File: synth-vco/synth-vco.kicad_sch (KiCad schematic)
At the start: 61 parts, among them J1 Conn_Coaxial, J2 Screw_Terminal_01x10, J3 Screw_Terminal_01x05, J4 Conn_Coaxial, U1 ADF4158, U2 BT09E, U3 ADP-2-10+, U4 DAT-15R5A-SP+, U5 OPA192IDGKT, Y3 CVCO55CW-0500-1000

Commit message: reorder: added components' footprints and symbols files to the repo directory instead of them being unorganized in my downloads folder
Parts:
- Y3: footprint CVCO55CW-0500-1000:XTAL_CVCO55CW-0500-1000 -> GPR_Radar_Footprints:XTAL_CVCO55CW-0500-1000
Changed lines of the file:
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@@
 			)
 		)
-		(property "Footprint" "CVCO55CW-0500-1000:XTAL_CVCO55CW-0500-1000"
+		(property "Footprint" "GPR_Radar_Footprints:XTAL_CVCO55CW-0500-1000"
 			(at 403.86 254 0)
 			(hide yes)
@@
 			)
 		)
-		(property "Datasheet" ""
+		(property "Datasheet" "https://www.crystek.com/Specification/CVCO55CW-0500-1000"
 			(at 403.86 254 0)
 			(hide yes)

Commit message: schematic-feat: made the schematic for external 12V buck to 6V + LDOs to 5V and 3V3 lines
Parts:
- added C23, C31: 4.7u, Capacitor_SMD:C_0603_1608Metric_Pad1.08x0.95mm_HandSolder, symbol Device:C
- added C24, C25, C27, C29, C30, C32: 10u, Capacitor_SMD:C_0603_1608Metric_Pad1.08x0.95mm_HandSolder, symbol Device:C
- added C26, C28: 22u, Capacitor_SMD:C_0603_1608Metric_Pad1.08x0.95mm_HandSolder, symbol Device:C
- added J5: Barrel_Jack, Connector_BarrelJack:BarrelJack_SwitchcraftConxall_RAPC10U_Horizontal, symbol Connector:Barrel_Jack
- added NT1: NetTie_2, NetTie:NetTie-2_SMD_Pad0.5mm, symbol Device:NetTie_2
- added R22: 10K, Resistor_SMD:R_0201_0603Metric_Pad0.64x0.40mm_HandSolder, symbol Device:R
- added R23: 2K, Resistor_SMD:R_0201_0603Metric_Pad0.64x0.40mm_HandSolder, symbol Device:R
- added R24, R25: 49.9K, Resistor_SMD:R_0201_0603Metric_Pad0.64x0.40mm_HandSolder, symbol Device:R
- added U6: TPSM53602RDAR, GPR_Radar_Footprints:IC_TPSM53603RDAR, symbol TPSM53602RDAR:TPSM53602RDAR
- added U7, U8: LT3045IMSE_TRPBF, GPR_Radar_Footprints:SOP65P490X110-13N, symbol LT3045IMSE_TRPBF:LT3045IMSE_TRPBF
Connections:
- net GND: now also C23.1, C24.1, C25.1, C26.1, C27.1, C28.1, C29.1, C30.1, C31.1, C32.1, J5.2, NT1.2, R24.2, R25.2, U6.10 (NC), U6.11 (NC), U6.15 (PGND), U6.15_1 (PGND), U6.15_10 (PGND), U6.15_11 (PGND), U6.15_2 (PGND), U6.15_3 (PGND), U6.15_4 (PGND), U6.15_5 (PGND), U6.15_6 (PGND), U6.15_7 (PGND), U6.15_8 (PGND), U6.15_9 (PGND), U6.3 (NC), U7.13 (EXP), U7.6 (ILIM), U7.9 (GND), U8.13 (EXP), U8.6 (ILIM), U8.9 (GND)
- net 12 renamed 12V
- net 5V renamed +5V_BT09E
- net +5V_BT09E: now also C32.2, U8.10 (OUTS), U8.11 (OUT), U8.12 (OUT); no longer U1.22 (VP)
- new net: NT1.1, R23.1, U6.12 (AGND)
- new net: R22.1, R23.2, U6.9 (FB)
- new net: C31.2, R25.1, U8.8 (SET)
- new net: C23.2, R24.1, U7.8 (SET)
- new net +12V_IN: C25.2, C27.2, J5.1, U6.1 (VIN), U6.14 (VIN), U6.2 (EN)
- new net +5V_VP: C24.2, U1.22 (VP), U7.10 (OUTS), U7.11 (OUT), U7.12 (OUT)
- new net +6V_PRE: C26.2, C28.2, C29.2, C30.2, R22.2, U6.7 (VOUT), U6.8 (VOUT), U7.1 (IN), U7.2 (IN), U7.3 (IN), U7.4 (EN/UV), U7.7 (PGFB), U8.1 (IN), U8.2 (IN), U8.3 (IN), U8.4 (EN/UV), U8.7 (PGFB)
- no-connect marks 0 -> 4

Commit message: add: boost 6V to 20V LT8570 schematic
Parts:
- added C33, C35, C38, C41, C44: 10u, Capacitor_SMD:C_0603_1608Metric_Pad1.08x0.95mm_HandSolder, symbol Device:C
- added C34, C36, C39, C42: 4.7u, Capacitor_SMD:C_0603_1608Metric_Pad1.08x0.95mm_HandSolder, symbol Device:C
- added C37, C40, C43: 0.47u, Capacitor_SMD:C_0603_1608Metric_Pad1.08x0.95mm_HandSolder, symbol Device:C
- added R26: 49.9K, Resistor_SMD:R_0201_0603Metric_Pad0.64x0.40mm_HandSolder, symbol Device:R
- added R27, R28, R29: 32.4K, Resistor_SMD:R_0201_0603Metric_Pad0.64x0.40mm_HandSolder, symbol Device:R
- added U10, U11, U12, U9: LT3045IMSE_TRPBF, GPR_Radar_Footprints:SOP65P490X110-13N, symbol LT3045IMSE_TRPBF:LT3045IMSE_TRPBF
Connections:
- net +6V_PRE: now also C33.2, C36.2, C39.2, C42.2, U10.1 (IN), U10.2 (IN), U10.3 (IN), U10.4 (EN/UV), U10.7 (PGFB), U11.1 (IN), U11.2 (IN), U11.3 (IN), U11.4 (EN/UV), U11.7 (PGFB), U12.1 (IN), U12.2 (IN), U12.3 (IN), U12.4 (EN/UV), U12.7 (PGFB), U9.1 (IN), U9.2 (IN), U9.3 (IN), U9.4 (EN/UV), U9.7 (PGFB)
- net 3V3: no longer FL1.2, U1.18 (SDVDD), U1.19 (DVDD), U1.6 (AVDD), U1.7 (AVDD), U1.8 (AVDD)
- net GND: now also C33.1, C34.1, C35.1, C36.1, C37.1, C38.1, C39.1, C40.1, C41.1, C42.1, C43.1, C44.1, R26.2, R27.2, R28.2, R29.2, U10.13 (EXP), U10.6 (ILIM), U10.9 (GND), U11.13 (EXP), U11.6 (ILIM), U11.9 (GND), U12.13 (EXP), U12.6 (ILIM), U12.9 (GND), U9.13 (EXP), U9.6 (ILIM), U9.9 (GND)
- new net: C34.2, R26.1, U9.8 (SET)
- new net: C40.2, R28.1, U11.8 (SET)
- new net: C43.2, R29.1, U12.8 (SET)
- new net: C37.2, R27.1, U10.8 (SET)
- new net +3V3_PLL_A: C38.2, U1.6 (AVDD), U1.7 (AVDD), U1.8 (AVDD), U10.10 (OUTS), U10.11 (OUT), U10.12 (OUT)
- new net +3V3_PLL_D: C41.2, U1.18 (SDVDD), U1.19 (DVDD), U11.10 (OUTS), U11.11 (OUT), U11.12 (OUT)
- new net +3V3_TCXO: C44.2, FL1.2, U12.10 (OUTS), U12.11 (OUT), U12.12 (OUT)
- new net +5V_ADL5611: C35.2, U9.10 (OUTS), U9.11 (OUT), U9.12 (OUT)
- no-connect marks 4 -> 8
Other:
- note added: "3V3 Lines"
- note added: "5V Lines"
- moved on the sheet: AT1, C1, C10, C11, C12, C13, C14, C15, C16, C17, C18, C19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

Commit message: add: 12V and 18V lines from 20V, BT09E changed to power amp, ADL5611 before power splitter
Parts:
- removed C18: 100pF, symbol Device:C
- removed C19: 10u, symbol Device:C
- removed L2: 3.9nH, Inductor_SMD:L_0201_0603Metric_Pad0.64x0.40mm_HandSolder, symbol Device:L
- removed U2: BT09E, Package_TO_SOT_SMD:SOT-89-3, symbol GPR_custom:BT09E
- added AR1: ADL5611ARKZ-R7, GPR_Radar_Footprints:AMP_ADL5611ARKZ-R7, symbol ADL5611ARKZ-R7:ADL5611ARKZ-R7
- added C45: 470n, Capacitor_SMD:C_0603_1608Metric_Pad1.08x0.95mm_HandSolder, symbol Device:C
- added C46: 0.1u, Capacitor_SMD:C_0603_1608Metric_Pad1.08x0.95mm_HandSolder, symbol Device:C
- added C47: 2.2n, Capacitor_SMD:C_0603_1608Metric_Pad1.08x0.95mm_HandSolder, symbol Device:C
- added C48: 47p, Capacitor_SMD:C_0603_1608Metric_Pad1.08x0.95mm_HandSolder, symbol Device:C
- added C49: 4.7u, Capacitor_SMD:C_0603_1608Metric_Pad1.08x0.95mm_HandSolder, symbol Device:C
- added C50, C52, C53, C54: 10n, Capacitor_SMD:C_0603_1608Metric_Pad1.08x0.95mm_HandSolder, symbol Device:C
- added C51, C55, C65: 10u, Capacitor_SMD:C_0603_1608Metric_Pad1.08x0.95mm_HandSolder, symbol Device:C
- added C56: 100n, Capacitor_SMD:C_0201_0603Metric_Pad0.64x0.40mm_HandSolder, symbol Device:C
- added C57, C59, C61, C63: 100n, Capacitor_SMD:C_0603_1608Metric_Pad1.08x0.95mm_HandSolder, symbol Device:C
- added C58, C60, C62, C64: 10p, Capacitor_SMD:C_0603_1608Metric_Pad1.08x0.95mm_HandSolder, symbol Device:C
- added C66, C68, C72: 100pF, symbol Device:C
- added C67: 9pF, symbol Device:C
- added C69: 1uF, symbol Device:C
- added C70: 10u, symbol Device:C
- added C71: 1.8pF, symbol Device:C
- added D1: D_Schottky, Diode_SMD:D_01005_0402Metric_Pad0.57x0.30mm_HandSolder, symbol Device:D_Schottky
- added FL4: LFCN-900+, Filter:Filter_Mini-Circuits_FV1206, symbol GPR_custom:LFCN-900+
- added L4: 47u, Inductor_SMD:L_0201_0603Metric_Pad0.64x0.40mm_HandSolder, symbol Device:L
- added L5: 82nH, Inductor_SMD:L_0201_0603Metric_Pad0.64x0.40mm_HandSolder, symbol Device:L
- added L6: 3.9nH, Inductor_SMD:L_0201_0603Metric_Pad0.64x0.40mm_HandSolder, symbol Device:L
- added R30: 10K, Resistor_SMD:R_0201_0603Metric_Pad0.64x0.40mm_HandSolder, symbol Device:R
- added R31: 56k, Resistor_SMD:R_0201_0603Metric_Pad0.64x0.40mm_HandSolder, symbol Device:R
- added R32: 226K, Resistor_SMD:R_0201_0603Metric_Pad0.64x0.40mm_HandSolder, symbol Device:R
- added R33: 6.19K, Resistor_SMD:R_0201_0603Metric_Pad0.64x0.40mm_HandSolder, symbol Device:R
- added R34: 1.15M, Resistor_SMD:R_0201_0603Metric_Pad0.64x0.40mm_HandSolder, symbol Device:R
- added R35, R37: 60.4K, Resistor_SMD:R_0201_0603Metric_Pad0.64x0.40mm_HandSolder, symbol Device:R
- added R36: 1.74M, Resistor_SMD:R_0201_0603Metric_Pad0.64x0.40mm_HandSolder, symbol Device:R
- added R38: 10, Resistor_SMD:R_0201_0603Metric_Pad0.64x0.40mm_HandSolder, symbol Device:R
- added R39, R41: 100, Resistor_SMD:R_01005_0402Metric_Pad0.57x0.30mm_HandSolder, symbol Device:R
- added R40: 68, Resistor_SMD:R_01005_0402Metric_Pad0.57x0.30mm_HandSolder, symbol Device:R
- added U13: LT8570EMS8E_TRPBF, GPR_Radar_Footprints:SOP65P490X110-9N, symbol LT8570EMS8E_TRPBF:LT8570EMS8E_TRPBF
- added U14, U15: LT3065EDDPBF, GPR_Radar_Footprints:DFN-10_DD, symbol LT3065EDDPBF:LT3065EDDPBF
- added U16: BT09E, Package_TO_SOT_SMD:SOT-89-3, symbol GPR_custom:BT09E
- C14: value 9pF -> 100pF
- C15: value 100pF -> 68pF
- C16: value 1.8pF -> 1.2nF
- L1: value 82nH -> 43nH
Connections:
- net 3V3 is gone; now on net +3V3_PLL_D: R15.2, R16.2, R17.2, R18.2, R19.2, R4.2, U4.13 (VDD), U4.6 (VDD), U4.9 (VDD)
- net +12V_IN: now also C45.2, L4.1, R30.2, U13.3 (VIN)
- net +3V3_PLL_A: now also C59.1, C60.1
- net +3V3_PLL_D: now also C56.1, C57.1, C58.1, C61.1, C62.1
- net +5V_ADL5611: now also C15.1, C16.2, C17.2, L1.2
- net +5V_BT09E: now also C68.2, C69.2, C70.2, L5.2; no longer C15.2, C17.2, L1.2
- net +5V_VP: now also C63.1, C64.1
- net GND: now also C15.2, AR1.2_4 (GND), C45.1, C46.1, C47.1, C48.1, C49.1, C51.1, C52.1, C53.1, C55.1, C56.2, C57.2, C58.2, C59.2, C60.2, C61.2, C62.2, C63.2, C64.2, C65.1, C67.1, C68.1, C69.1, C70.1, C71.1, FL4.2 (GND), FL4.4 (GND), R31.1, R35.2, R37.2, R39.1, R41.1, U13.8 (SYNC), U13.9 (GND), U14.11 (GND), U14.5 (IMAX), U14.7 (GND), U15.11 (GND), U15.5 (IMAX), U15.7 (GND), U16.2 (GND); no longer C14.1, C15.1
- net at C21.2: now also R39.2, R40.1; no longer J4.1 (In)
- net at C14.2: now also FL3.1 (IN); no longer C13.2
- net at L1.1: now also C14.1, AR1.3 (RFOUT)
- net 12V renamed +12V_VCO
- net +12V_VCO: now also C50.2, C51.2, R34.1, U14.10 (OUT), U14.9 (OUT)
- net 20V renamed +18V_OPA
- net +18V_OPA: now also C54.2, C55.2, R36.1, U15.10 (OUT), U15.9 (OUT)
- new net: C66.2, C67.2, U16.1 (RF_in)
- new net: L5.1, L6.1, U16.3 (RF_out)
- new net: C48.2, R33.1, U13.2 (VC)
- new net: C47.2, R33.2
- new net: C66.1, R40.2, R41.2
- new net: C71.2, C72.1, L6.2
- new net: C72.2, FL4.1 (IN)
- new net: C49.2, D1.1 (K), R32.1, R38.2
- new net: AR1.1 (RFIN), C13.2
- new net: D1.2 (A), L4.2, U13.4 (SW)
- new net: C54.1, R36.2, R37.1, U15.8 (ADJ)
- new net: C46.2, U13.7 (SS)
- new net: C53.2, U15.6 (REF/BYP)
- new net: R31.2, U13.6 (RT)
- new net: FL4.3 (OUT), J4.1 (In)
- new net: R30.1, U13.5 (~{SHDN})
- new net: C52.2, U14.6 (REF/BYP)
- new net: C50.1, R34.2, R35.1, U14.8 (ADJ)
- new net: R32.2, U13.1 (FBX)
- new net +20V_PRE: C65.2, R38.1, U14.1 (IN), U14.2 (IN), U14.3 (~{SHDN}), U15.1 (IN), U15.2 (IN), U15.3 (~{SHDN})
- no-connect marks 8 -> 10
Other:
- note added: "12V Line"
- note added: "18V Line"
- note added: "Boost to 20V"
- moved on the sheet: AT1, C1, C10, C11, C12, C2, C20, C21, C22, C3, C4, C5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

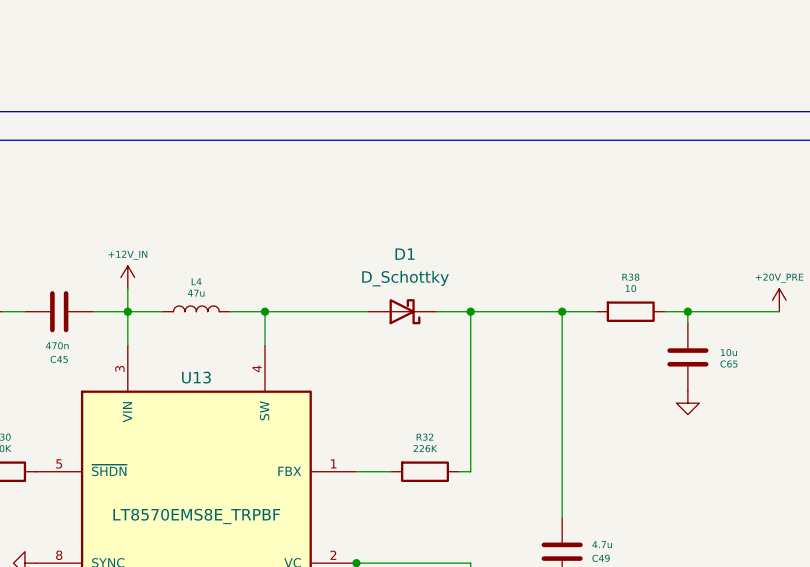
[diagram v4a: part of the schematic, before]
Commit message: chore: switched default schottky diode to MSS1P4
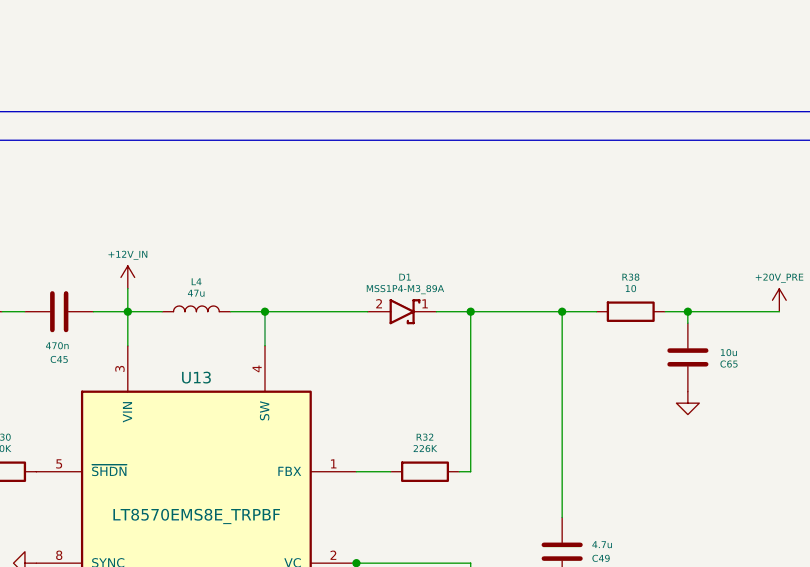
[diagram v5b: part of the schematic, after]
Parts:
- removed D1: D_Schottky, Diode_SMD:D_01005_0402Metric_Pad0.57x0.30mm_HandSolder, symbol Device:D_Schottky
- added D1: MSS1P4-M3_89A, GPR_Radar_Footprints:DIODE_MSS1P4-M3_89A, symbol MSS1P4-M3_89A:MSS1P4-M3_89A
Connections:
- net at C49.2, R32.1, R38.2: now also D1.1
- net at L4.2, U13.4 (SW): now also D1.2
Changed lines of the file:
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@@
+	)
+	(symbol
+		(lib_id "MSS1P4-M3_89A:MSS1P4-M3_89A")
+		(at 92.71 138.43 0)
+		(unit 1)
+		(body_style 1)
+		(exclude_from_sim no)
+		(in_bom yes)
+		(on_board yes)
+		(in_pos_files yes)
+		(dnp no)
+		(fields_autoplaced yes)
+		(property "Reference" "D1"
+			(at 93.0275 134.62 0)
+			(show_name no)
+			(do_not_autoplace no)
+			(effects
+				(font
+					(size 0.762 0.762)
+				)
+			)
+		)
+		(property "Value" "MSS1P4-M3_89A"
+			(at 93.0275 135.89 0)
+			(show_name no)
+			(do_not_autoplace no)
+			(effects
+				(font
+					(size 0.762 0.762)
+				)
+			)
+		)
+		(property "Footprint" "GPR_Radar_Footprints:DIODE_MSS1P4-M3_89A"
+			(at 92.71 157.48 0)
+			(hide yes)
+			(show_name no)
+			(do_not_autoplace no)
+			(effects
+				(font
+					(size 1.27 1.27)
+				)
+				(justify bottom)
+			)
+		)
+		(property "Datasheet" ""
+			(at 92.71 138.43 0)
+			(hide yes)
+			(show_name no)
+			(do_not_autoplace no)
+			(effects
+				(font
+					(size 1.27 1.27)
+				)
+			)
+		)
+		(property "Description" "Diode Schottky 40 V 1A Surface Mount MicroSMP (DO-219AD)"
+			(at 92.71 154.94 0)
+			(hide yes)
+			(show_name no)
+			(do_not_autoplace no)
+			(effects
+				(font
+					(size 1.27 1.27)
+				)
+				(justify bottom)
+			)
+		)
+		(property "MF" "Vishay Semiconductor"
+			(at 92.71 144.78 0)
+			(hide yes)
+			(show_name no)
+			(do_not_autoplace no)
+			(effects
+				(font
+					(size 1.27 1.27)
+				)
+				(justify bottom)
+			)
+		)
+		(property "PACKAGE" "MicroSMP Vishay Semiconductor"
+			(at 93.98 132.08 0)
+			(hide yes)
+			(show_name no)
+			(do_not_autoplace no)
+			(effects
+				(font
+					(size 1.27 1.27)
+				)
+				(justify bottom)
+			)
+		)
+		(property "Price" "None"
+			(at 91.44 160.02 0)
+			(hide yes)
+			(show_name no)
+			(do_not_autoplace no)
+			(effects
+				(font
+					(size 1.27 1.27)
+				)
+				(justify bottom)
+			)
+		)
+		(property "Package" "MicroSMP Vishay Semiconductor"
+			(at 92.71 134.62 0)
+			(hide yes)
+			(show_name no)
+			(do_not_autoplace no)
+			(effects
+				(font
+					(size 1.27 1.27)
+				)
+				(justify bottom)
+			)
+		)
+		(property "Check_prices" "https://www.snapeda.com/parts/MSS1P4-M3/89A/Vishay/view-part/?ref=eda"
+			(at 92.71 149.86 0)
+			(hide yes)
+			(show_name no)
+			(do_not_autoplace no)
+			(effects
+				(font
+					(size 1.27 1.27)
+				)
+				(justify bottom)
+			)
+		)
+		(property "SnapEDA_Link" "https://www.snapeda.com/parts/MSS1P4-M3/89A/Vishay/view-part/?ref=snap"
+			(at 92.71 152.4 0)
+			(hide yes)
+			(show_name no)
+			(do_not_autoplace no)
+			(effects
+				(font
+					(size 1.27 1.27)
+				)
+				(justify bottom)
+			)
+		)
+		(property "MP" "MSS1P4-M3/89A"
+			(at 92.71 129.54 0)
+			(hide yes)
+			(show_name no)
+			(do_not_autoplace no)
+			(effects
+				(font
+					(size 1.27 1.27)
+				)
+				(justify bottom)
+			)
+		)
+		(property "Purchase-URL" "https://www.snapeda.com/api/url_track_click_mouser/?unipart_id=2014293&manufacturer=Vishay Semiconductor&part_name=MSS1P4-M3/89A&search_term=mss1p4-m3/89a"
+			(at 93.98 147.32 0)
+			(hide yes)
+			(show_name no)
+			(do_not_autoplace no)
+			(effects
+				(font
+					(size 1.27 1.27)
+				)
+				(justify bottom)
+			)
+		)
+		(property "Availability" "In Stock"
+			(at 93.98 127 0)
+			(hide yes)
+			(show_name no)
+			(do_not_autoplace no)
+			(effects
+				(font
+					(size 1.27 1.27)
+				)
+				(justify bottom)
+			)
+		)
+		(pin "1"
+		)
+		(pin "2"
+		)
+		(instances
+			(project "synth-vco"
+				(path "/73cd0915-f93d-4399-bfe5-6d917fa8cde7"
+					(reference "D1")
+					(unit 1)
+				)
+			)
+		)
 	)
 	(symbol
@@
 					(unit 1)
 				)
-			)
-		)
-	)
-	(symbol
-		(lib_id "Device:D_Schottky")
-		(at 92.71 138.43 180)
-		(unit 1)
-		(body_style 1)
-		(exclude_from_sim no)
-		(in_bom yes)
-		(on_board yes)
-		(in_pos_files yes)
-		(dnp no)
-		(fields_autoplaced yes)
-		(property "Reference" "D1"
-			(at 93.0275 132.08 0)
-			(show_name no)
-			(do_not_autoplace no)
-			(effects
-				(font
-					(size 1.27 1.27)
-				)
-			)
-		)
-		(property "Value" "D_Schottky"
-			(at 93.0275 134.62 0)
-			(show_name no)
-			(do_not_autoplace no)
-			(effects
-				(font
-					(size 1.27 1.27)
-				)
-			)
-		)
-		(property "Footprint" "Diode_SMD:D_01005_0402Metric_Pad0.57x0.30mm_HandSolder"
-			(at 92.71 138.43 0)
-			(hide yes)
-			(show_name no)
-			(do_not_autoplace no)
-			(effects
-				(font
-					(size 1.27 1.27)
-				)
-			)
-		)
-		(property "Datasheet" ""
-			(at 92.71 138.43 0)
-			(hide yes)
-			(show_name no)
-			(do_not_autoplace no)
-			(effects
-				(font
-					(size 1.27 1.27)
-				)
-			)
-		)
-		(property "Description" "Schottky diode"
-			(at 92.71 138.43 0)
-			(hide yes)
-			(show_name no)
-			(do_not_autoplace no)
-			(effects
-				(font
-					(size 1.27 1.27)
-				)
-			)
-		)
-		(pin "2"
-		)
-		(pin "1"
-		)
-		(instances
-			(project "synth-vco"
-				(path "/73cd0915-f93d-4399-bfe5-6d917fa8cde7"
-					(reference "D1")
-					(unit 1)
-				)
